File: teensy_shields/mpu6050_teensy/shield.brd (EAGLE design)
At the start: 33 x 59.4 mm, 2 parts

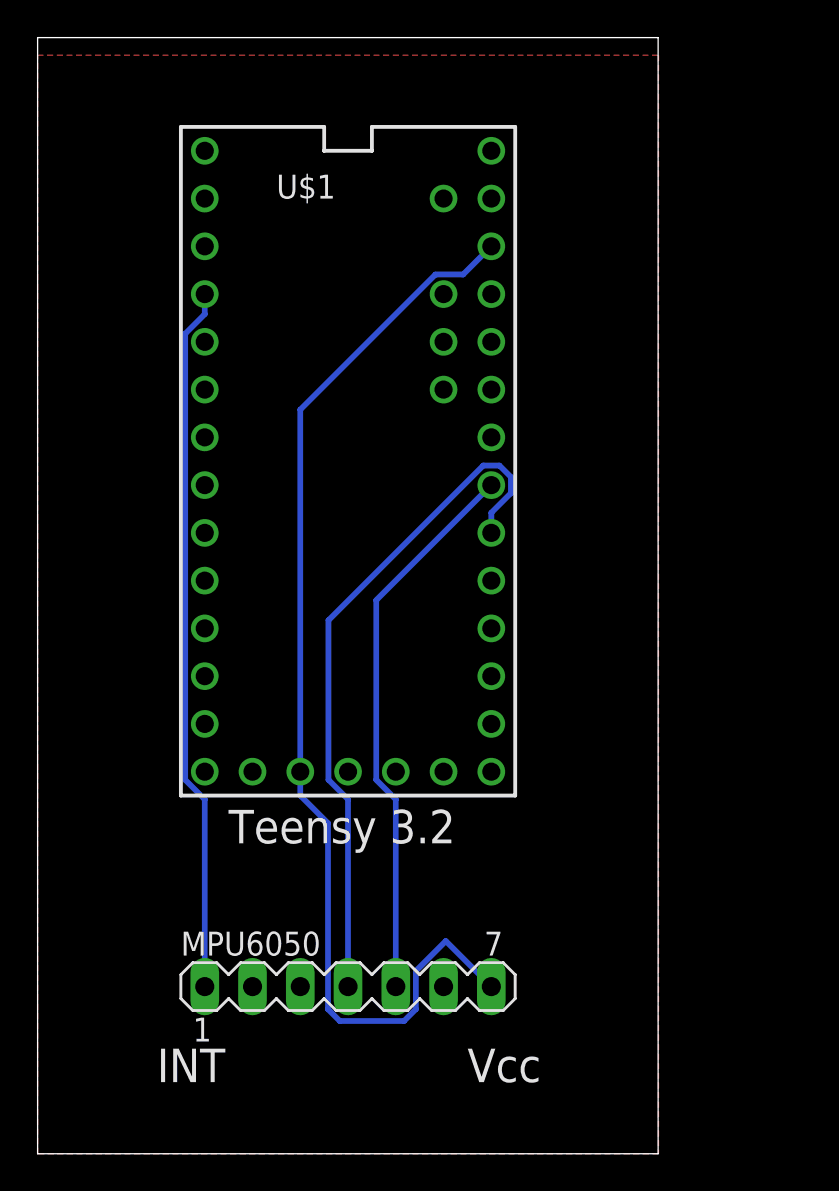
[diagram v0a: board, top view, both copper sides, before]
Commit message: Cleaned up board
Added a pulldown resistor to the i2c channel select pin and cleaned up the the board.
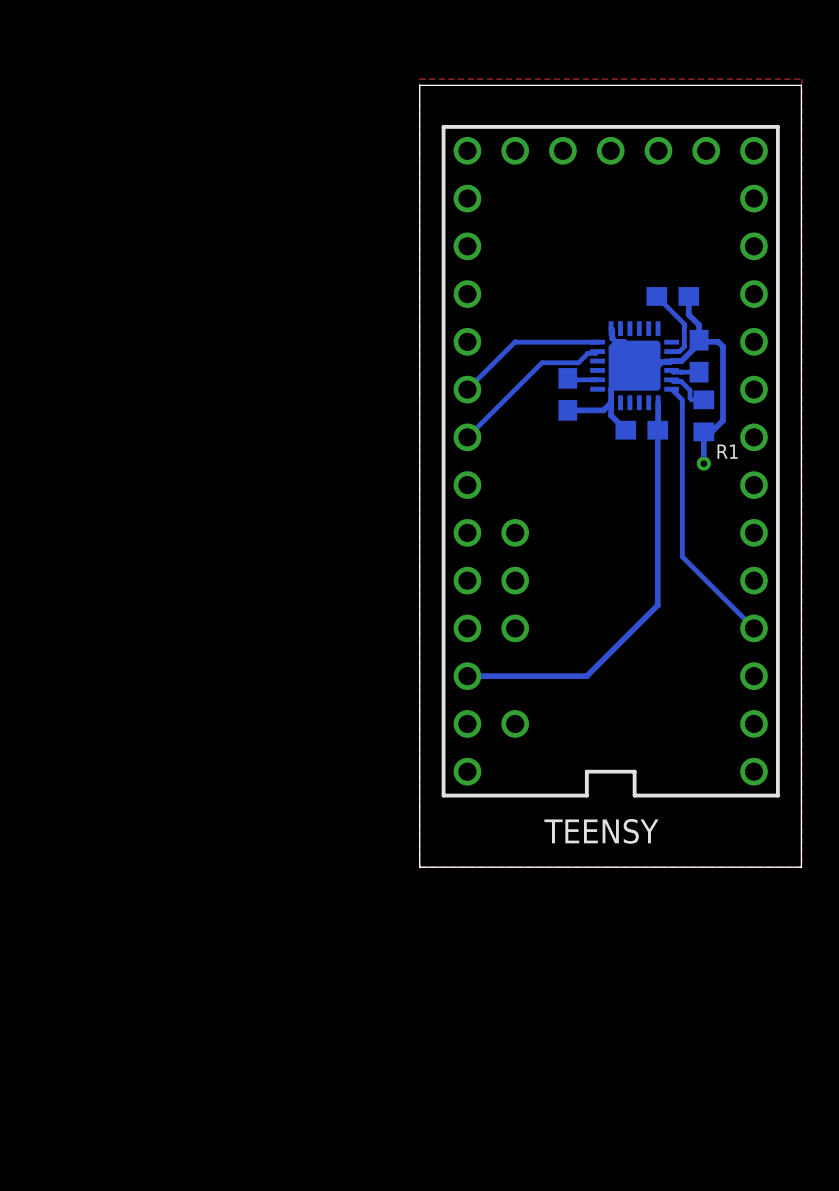
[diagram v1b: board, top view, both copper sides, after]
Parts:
- removed U$1: TEENSY_3.1-3.2_ALL_PINS, Teensy:TEENSY_3.0-3.2&LC_ALL_PINS
- added C1, C2: 0.1uF, SparkFun-Capacitors:0603
- added C3: 2.2nF, SparkFun-Capacitors:0603
- added C4: 10nF, SparkFun-Capacitors:0603
- added R1: (no value), eagle-ltspice:R0603
- added TEENSY: TEENSY_3.1-3.2_ALL_PINS, Teensy:TEENSY_3.0-3.2&LC_ALL_PINS
- MPU6050: value (none) -> MPU6050; device con-lstb:MA07-1 -> invensense:QFN50P400X400X95-25T265X275N
- moved MPU6050 36.4 mm to (31.8, 82.5), flipped to the bottom, turned to 180 degrees
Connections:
- new net N$1: C3.1, MPU6050.20
- new net N$2: C1.1, MPU6050.10
- new net N$3: C4.1, MPU6050.8
- new net N$4: MPU6050.11, R1.1
- net AGND: now also TEENSY.AGND; no longer U$1.AGND
- net AREF: now also TEENSY.AREF; no longer U$1.AREF
- net GND: now also C1.2, C2.2, C3.2, C4.2, MPU6050.1, MPU6050.18, MPU6050.25, MPU6050.9, R1.2, TEENSY.GND, TEENSY.GND1; no longer MPU6050.6, U$1.GND, U$1.GND1
- net INT: now also MPU6050.12, TEENSY.2; no longer MPU6050.1, U$1.2
- net SCL: now also MPU6050.23, TEENSY.19/A5; no longer MPU6050.5, U$1.19/A5
- net SDA: now also MPU6050.24, TEENSY.18/A4; no longer MPU6050.4, U$1.18/A4
- net VBAT: now also TEENSY.VBAT; no longer U$1.VBAT
- net VCC: now also C2.1, MPU6050.13, TEENSY.3.3V, TEENSY.3.3V1; no longer MPU6050.7, U$1.3.3V, U$1.3.3V1
- net VIN: now also TEENSY.VIN; no longer U$1.VIN
- net VUSB: now also TEENSY.VUSB; no longer U$1.VUSB
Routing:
- net VCC: track 59.2 -> 22.5 mm
- net SDA: track 36.7 -> 7.98 mm
- net GND: track 0.00 -> 24.4 mm, vias 0 -> 1
- net INT: track 37.7 -> 14.5 mm
- net SCL: track 29.6 -> 8.81 mm
- net N$3: track 0.00 -> 4.08 mm
- net N$4: track 0.00 -> 2.40 mm
- net N$1: track 0.00 -> 1.62 mm
- net N$2: track 0.00 -> 1.50 mm
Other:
- board size 33 x 59.4 mm -> 20.3 x 41.6 mm
- board text added: "R1"
- board text removed: "INT"
- board text removed: "Teensy 3.2"
- board text removed: "Vcc"

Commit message: Switched files
Corrected file directories
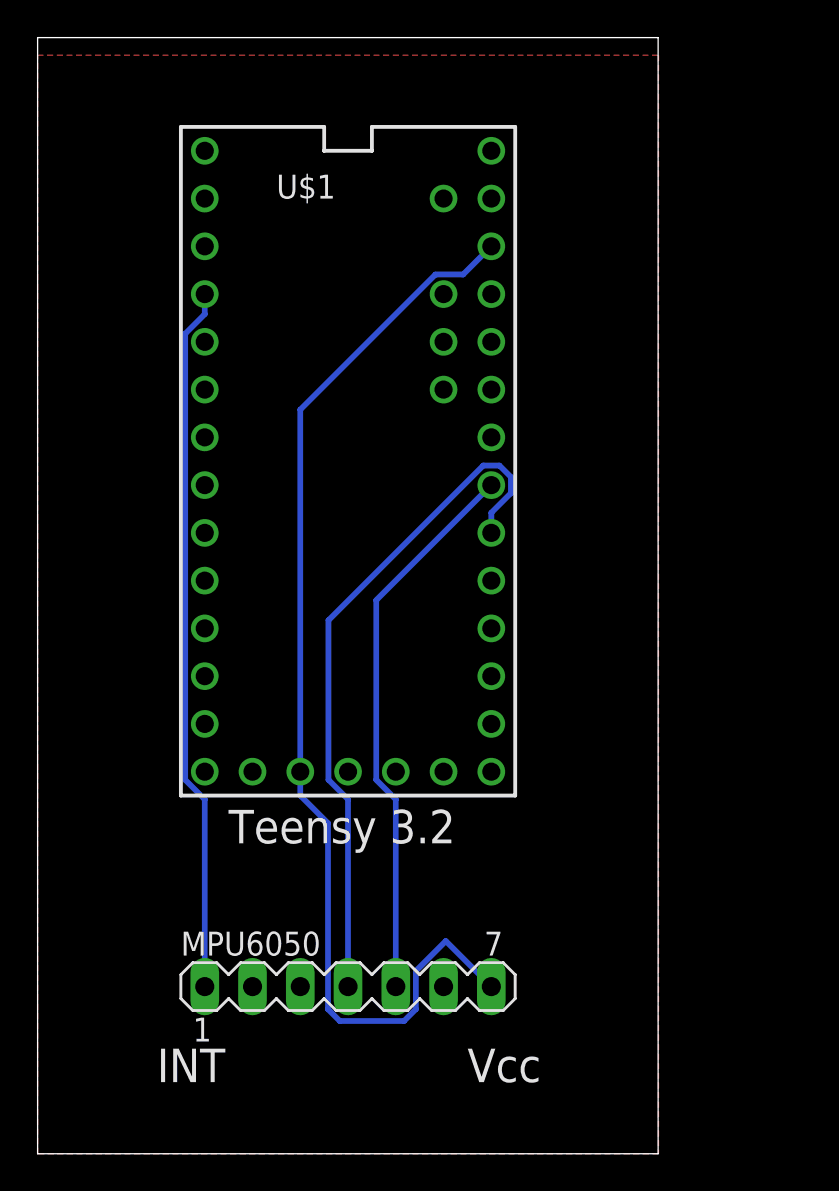
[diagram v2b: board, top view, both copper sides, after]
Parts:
- removed C1, C2: 0.1uF, SparkFun-Capacitors:0603
- removed C3: 2.2nF, SparkFun-Capacitors:0603
- removed C4: 10nF, SparkFun-Capacitors:0603
- removed R1: (no value), eagle-ltspice:R0603
- removed TEENSY: TEENSY_3.1-3.2_ALL_PINS, Teensy:TEENSY_3.0-3.2&LC_ALL_PINS
- added U$1: TEENSY_3.1-3.2_ALL_PINS, Teensy:TEENSY_3.0-3.2&LC_ALL_PINS
- MPU6050: value MPU6050 -> (none); device invensense:QFN50P400X400X95-25T265X275N -> con-lstb:MA07-1
- moved MPU6050 36.4 mm to (16.5, 49.5), flipped to the top, turned to 0 degrees
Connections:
- removed net N$1: C3.1, MPU6050.20
- removed net N$2: C1.1, MPU6050.10
- removed net N$3: C4.1, MPU6050.8
- removed net N$4: MPU6050.11, R1.1
- net AGND: now also U$1.AGND; no longer TEENSY.AGND
- net AREF: now also U$1.AREF; no longer TEENSY.AREF
- net GND: now also MPU6050.6, U$1.GND, U$1.GND1; no longer C1.2, C2.2, C3.2, C4.2, MPU6050.1, MPU6050.18, MPU6050.25, MPU6050.9, R1.2, TEENSY.GND, TEENSY.GND1
- net INT: now also MPU6050.1, U$1.2; no longer MPU6050.12, TEENSY.2
- net SCL: now also MPU6050.5, U$1.19/A5; no longer MPU6050.23, TEENSY.19/A5
- net SDA: now also MPU6050.4, U$1.18/A4; no longer MPU6050.24, TEENSY.18/A4
- net VBAT: now also U$1.VBAT; no longer TEENSY.VBAT
- net VCC: now also MPU6050.7, U$1.3.3V, U$1.3.3V1; no longer C2.1, MPU6050.13, TEENSY.3.3V, TEENSY.3.3V1
- net VIN: now also U$1.VIN; no longer TEENSY.VIN
- net VUSB: now also U$1.VUSB; no longer TEENSY.VUSB
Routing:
- net VCC: track 22.5 -> 59.2 mm
- net SDA: track 7.98 -> 36.7 mm
- net GND: track 24.4 -> 0.00 mm, vias 1 -> 0
- net INT: track 14.5 -> 37.7 mm
- net SCL: track 8.81 -> 29.6 mm
- net N$3: track 4.08 -> 0.00 mm
- net N$4: track 2.40 -> 0.00 mm
- net N$1: track 1.62 -> 0.00 mm
- net N$2: track 1.50 -> 0.00 mm
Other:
- board size 20.3 x 41.6 mm -> 33 x 59.4 mm
- board text added: "INT"
- board text added: "Teensy 3.2"
- board text added: "Vcc"
- board text removed: "R1"
